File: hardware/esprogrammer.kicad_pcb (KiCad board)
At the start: 2 copper layers, 36.1 x 20.5 mm, 22 parts, among them P1 USB_OTG, P2 CONN_02X03, SW1 SW_PUSH, SW2 SW_PUSH, U1 AP1117, U2 CP2102

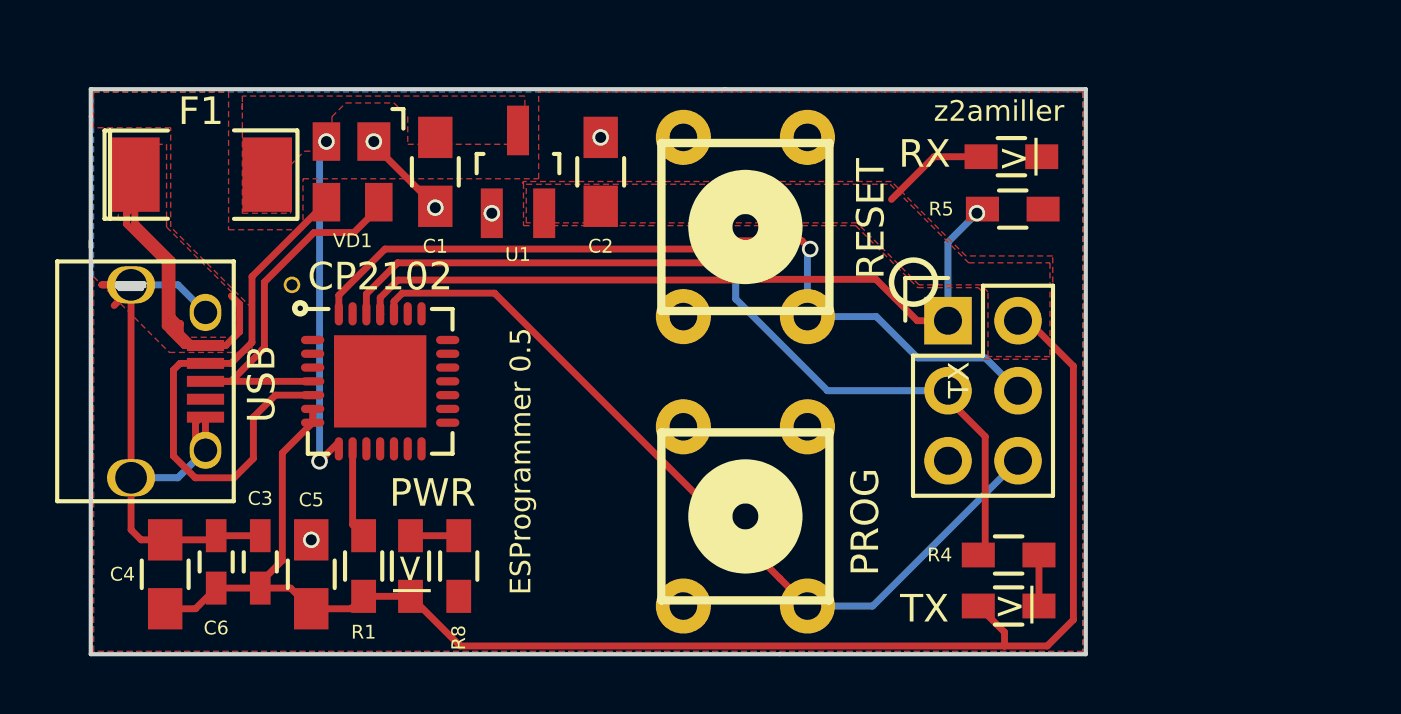
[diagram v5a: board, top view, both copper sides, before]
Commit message: Programmer 0.6 - cleanup and use reflow size pads.
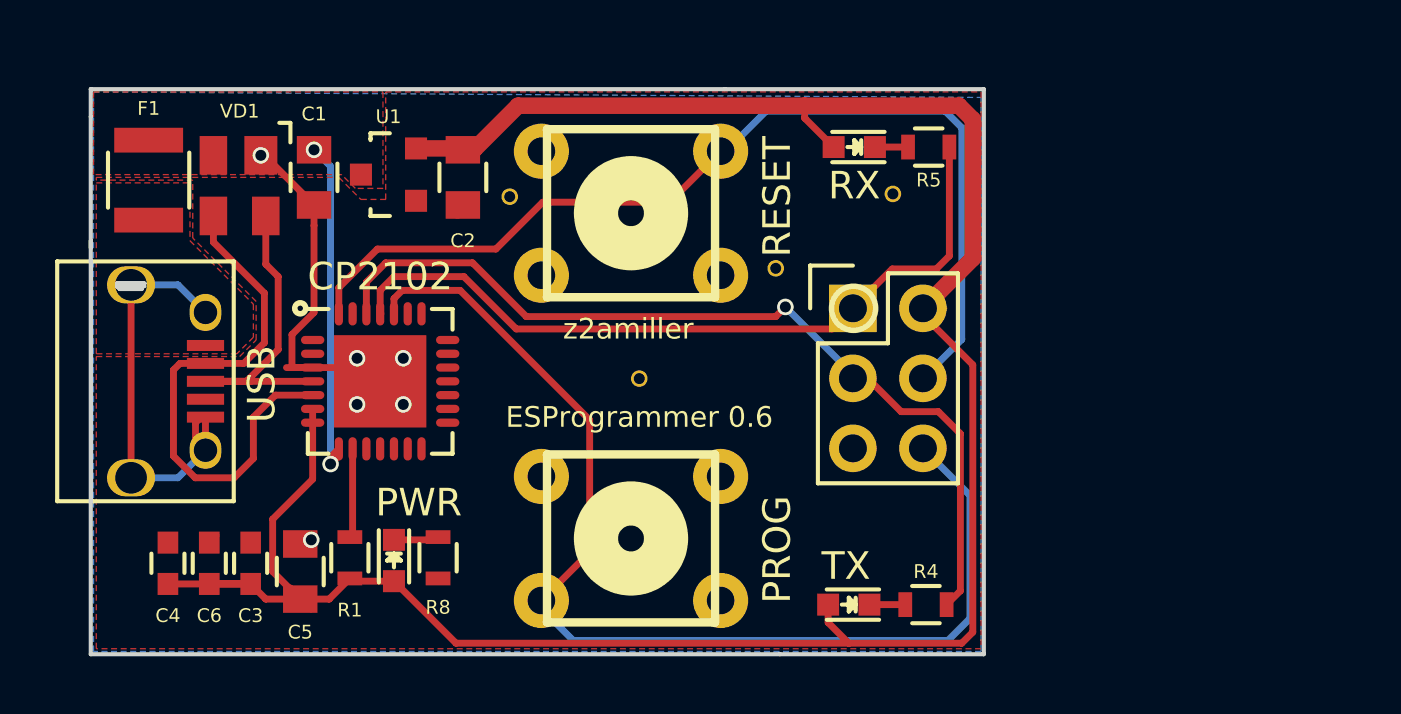
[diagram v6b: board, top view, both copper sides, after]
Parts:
- removed the REF** at (166.3, 94.6)
- added REF**: SolderWirePad_single_0-8mmDrill, Wire_Connections_Bridges:small_via, F.Cu at (174.2, 91.4)
- added REF**: SolderWirePad_single_0-8mmDrill, Wire_Connections_Bridges:small_via, F.Cu at (178.9, 98.0)
- added REF**: SolderWirePad_single_0-8mmDrill, Wire_Connections_Bridges:small_via, F.Cu at (183.8, 94.0)
- added REF**: SolderWirePad_single_0-8mmDrill, Wire_Connections_Bridges:small_via, F.Cu at (188.1, 91.3)
- C1, C2, C5: footprint Capacitors_SMD:C_0805_HandSoldering -> Capacitors_SMD:C_0805
- C3, C6: footprint Capacitors_SMD:C_0603_HandSoldering -> Capacitors_SMD:C_0603
- C4: footprint Capacitors_SMD:C_0805_HandSoldering -> Capacitors_SMD:C_0603
- D1, D2, D5: footprint Resistors_SMD:R_0603_HandSoldering -> LEDs:LED_0603
- F1: footprint SMD_Packages:SMD-2010_Pol -> Resistors_SMD:R_1210
- R1, R4, R5, R8: footprint Resistors_SMD:R_0603_HandSoldering -> Resistors_SMD:R_0603
- U1: footprint TO_SOT_Packages_SMD:SOT-23_Handsoldering -> TO_SOT_Packages_SMD:SOT-23
- moved D1 5.80 mm to (186.5, 106.2)
- moved D2 5.71 mm to (186.7, 89.6)
- moved C2 5.00 mm to (172.5, 90.7), turned to 270 degrees
- moved U1 4.70 mm to (169.8, 90.6), turned to 90 degrees
- moved C1 4.40 mm to (167.1, 90.7)
- moved SW2 4.23 mm to (178.6, 103.8), turned to 90 degrees
- moved SW1 4.18 mm to (178.6, 92.0), turned to 270 degrees
- moved VD1 4.13 mm to (164.4, 91.0)
- moved R5 3.79 mm to (189.4, 89.6), turned to 0 degrees
- moved R4 3.50 mm to (189.3, 106.2), turned to 0 degrees
- moved P2 3.48 mm to (186.7, 95.5)
- moved F1 1.91 mm to (161.1, 90.8), turned to 90 degrees
- moved R8 0.81 mm to (171.6, 104.5)
- moved D5 0.63 mm to (170.0, 104.6)
- moved R1 0.58 mm to (168.4, 104.5)
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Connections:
- SW1 pad 4: (no net) -> GND
- SW2 pad 4: (no net) -> GND
- U2 pad 29: (no net) -> GND
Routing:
- net +3V3: track 59.8 -> 87.2 mm
- net Net-(F1-Pad1): track 20.6 -> 0.46 mm
- net ESP_RST: track 30.1 -> 40.5 mm
- net GND: track 30.6 -> 37.5 mm, vias 5 -> 6
- net DTR: track 30.0 -> 36.1 mm, vias 1 -> 0
- net D+: track 14.4 -> 12.0 mm
- net Net-(D2-Pad1): track 0.00 -> 1.20 mm
- net TXD: track 31.6 -> 32.7 mm
- net RXD: track 26.7 -> 27.7 mm, vias 1 -> 0
- net Net-(D1-Pad1): track 1.85 -> 1.30 mm
- removed copper zone on F.Cu, net +3V3
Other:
- board size 36.1 x 20.5 mm -> 32.4 x 20.5 mm
- net class 3v3 added: clearance 0.2, trace_width 0.6, via_dia 0.8, via_drill 0.6
- board text added: "ESProgrammer 0.6"
- board text removed: ">|"
- board text removed: "ESProgrammer 0.5"
